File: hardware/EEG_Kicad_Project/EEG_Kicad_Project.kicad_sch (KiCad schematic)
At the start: 0 parts

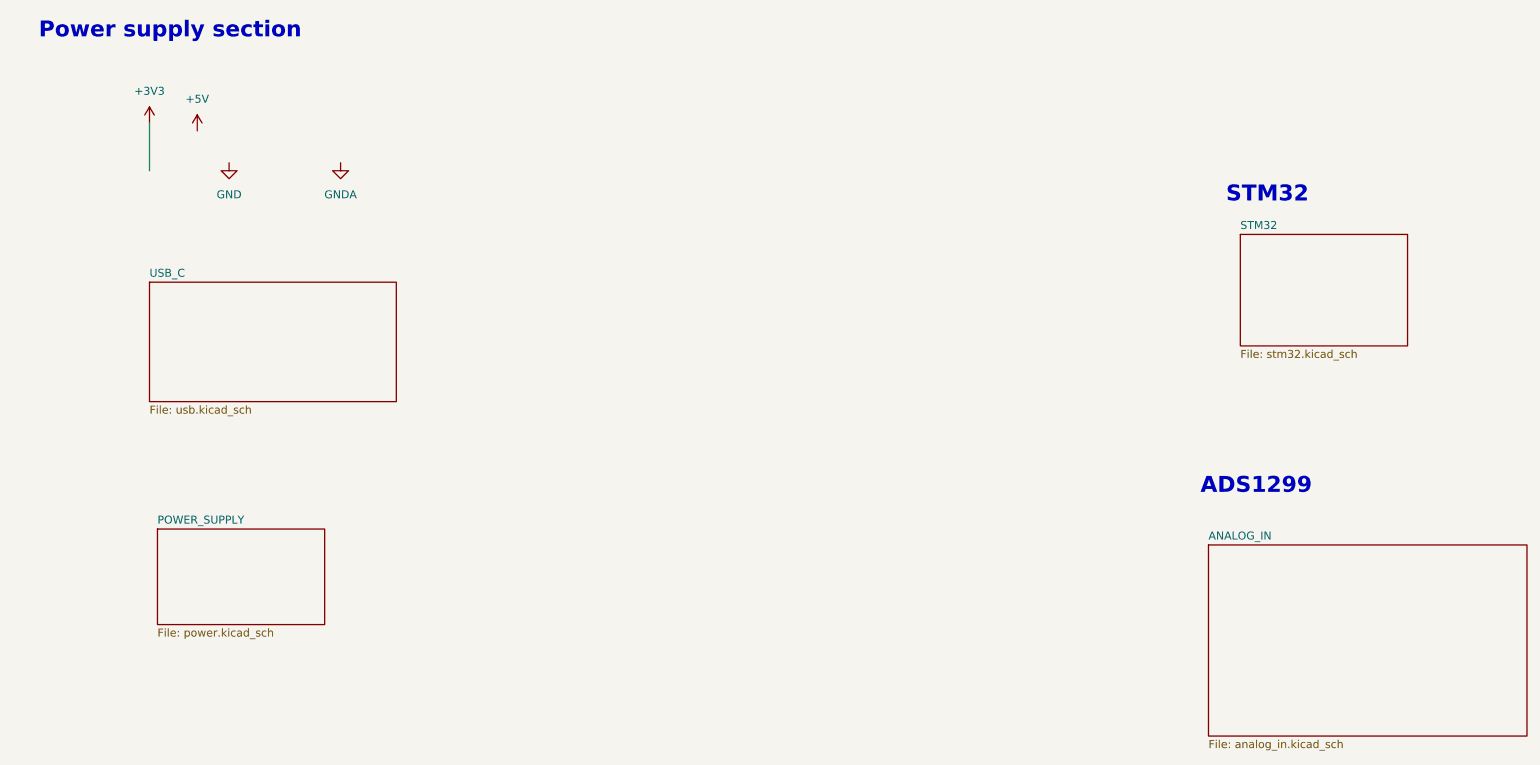
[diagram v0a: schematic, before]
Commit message: Readme change, add -5V, some organizational changes
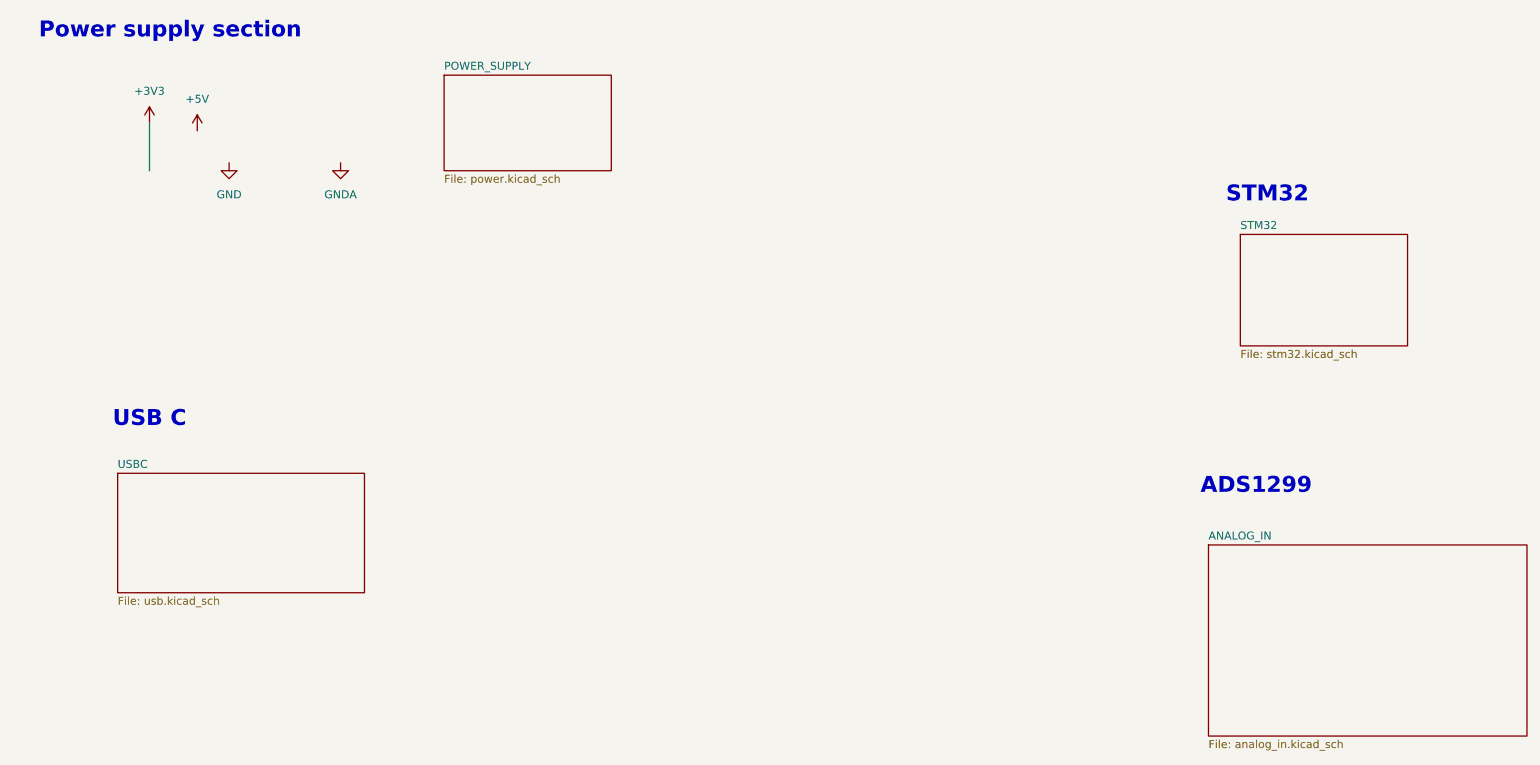
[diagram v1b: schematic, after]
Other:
- sheet USB_C renamed USBC
- note added: "USB C"
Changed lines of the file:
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@@
 	(generator_version "9.0")
 	(paper "A4")
+	(text "USB C"
+		(exclude_from_sim no)
+		(at 35.56 80.264 0)
+		(effects
+			(font
+				(size 2.54 2.54)
+				(thickness 0.508)
+				(bold yes)
+				(color 0 0 194 1)
+			)
+		)
+	)
 	(text "ADS1299"
 		(exclude_from_sim no)
@@
 	)
 	(sheet
-		(at 35.56 58.42)
+		(at 30.48 88.9)
 		(size 39.37 19.05)
 		(exclude_from_sim no)
@@
 			(color 0 0 0 0.0000)
 		)
-		(property "Sheetname" "USB_C"
-			(at 35.56 57.7084 0)
+		(property "Sheetname" "USBC"
+			(at 30.48 88.1884 0)
 			(effects
 				(font
@@
 		)
 		(property "Sheetfile" "usb.kicad_sch"
-			(at 35.56 78.0546 0)
+			(at 30.48 108.5346 0)
 			(effects
 				(font
@@
 	)
 	(sheet
-		(at 36.83 97.79)
+		(at 82.55 25.4)
 		(size 26.67 15.24)
 		(exclude_from_sim no)
@@
 		)
 		(property "Sheetname" "POWER_SUPPLY"
-			(at 36.83 97.0784 0)
+			(at 82.55 24.6884 0)
 			(effects
 				(font
@@
 		)
 		(property "Sheetfile" "power.kicad_sch"
-			(at 36.83 113.6146 0)
-			(effects
-				(font
+			(at 82.55 41.2246 0)
+			(effects
+				(font
